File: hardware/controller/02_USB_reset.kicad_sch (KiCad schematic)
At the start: 18 parts, among them J2 USB-C native USB2, Q2 MMBT3904 VBUS sense, U2 TPS2553DBVR, U3 USBLC6-2SC6, U4 TLV803EA30DBZR

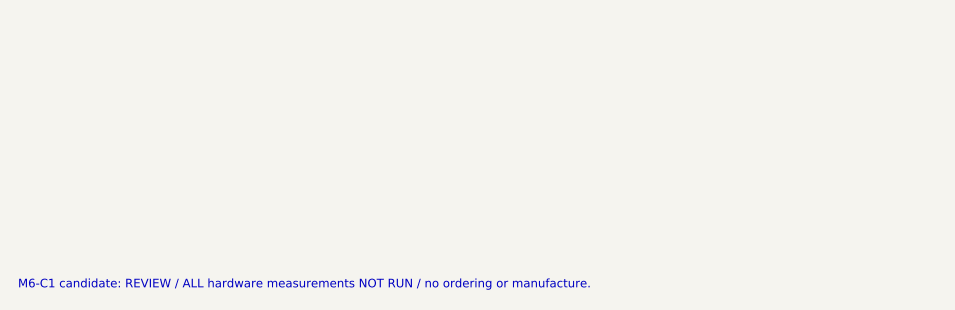
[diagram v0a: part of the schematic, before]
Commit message: M6-C1R1: protect pack identity input and review USB ESD topology
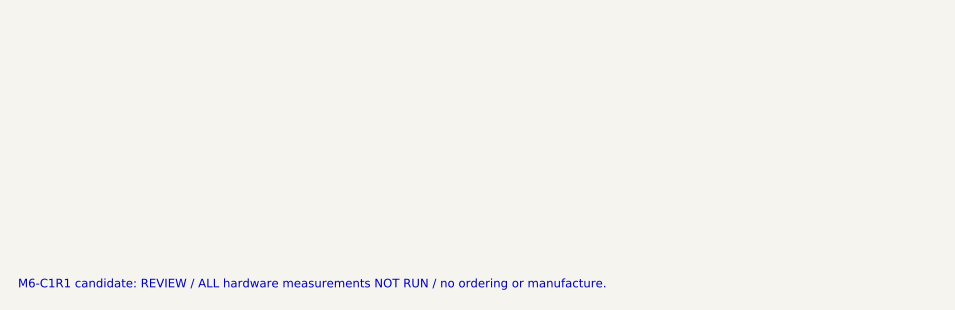
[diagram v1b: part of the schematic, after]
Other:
- note added: "M6-C1R1 candidate: REVIEW / ALL hardware measurements NOT RUN / no ordering or manufacture."
- note removed: "M6-C1 candidate: REVIEW / ALL hardware measurements NOT RUN / no ordering or manufacture."
